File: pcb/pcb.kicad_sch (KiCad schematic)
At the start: 29 parts

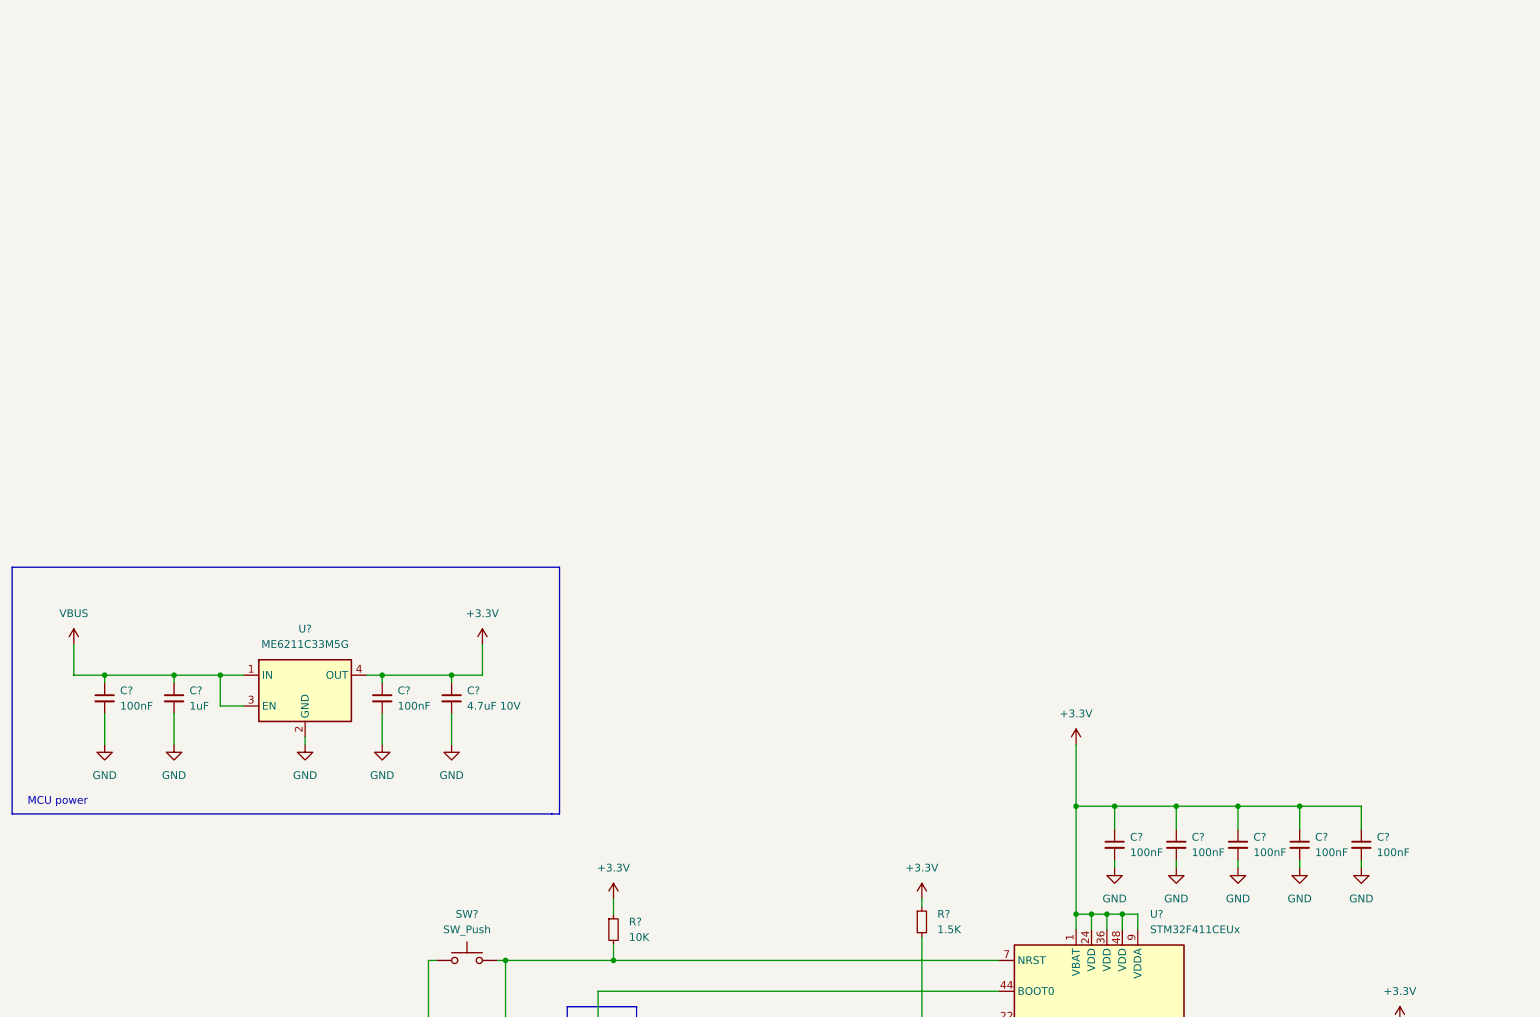
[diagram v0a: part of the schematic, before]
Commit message: add power tree
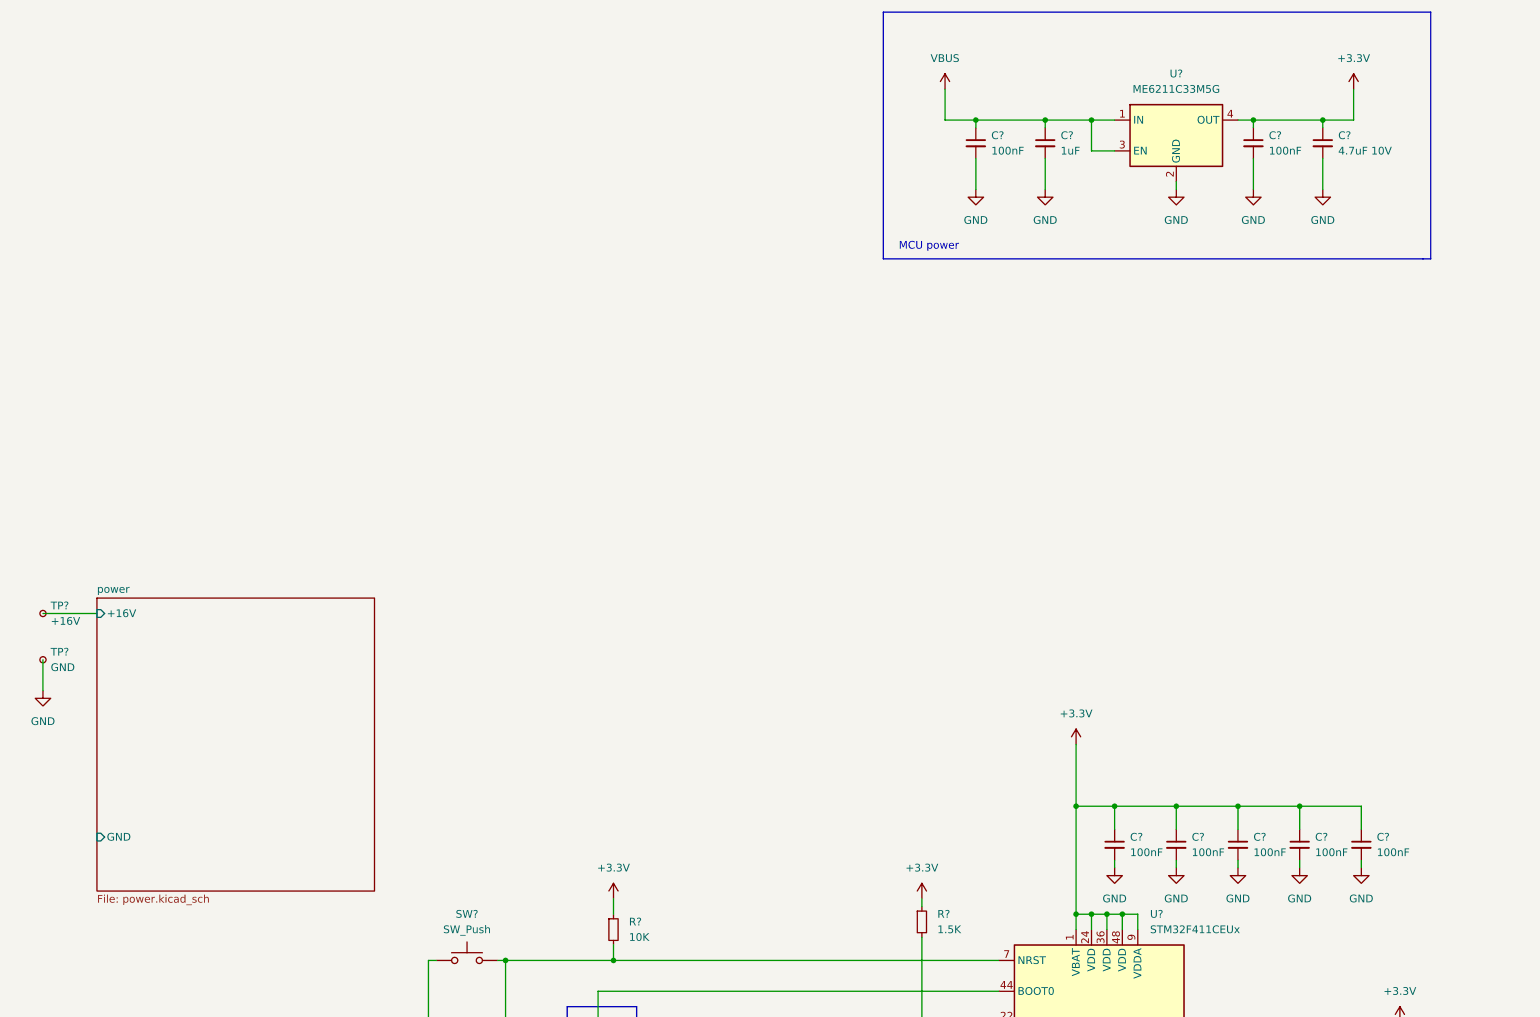
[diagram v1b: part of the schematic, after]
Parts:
- added TP?: GND, symbol Connector:TestPoint_Small
- added TP?: +16V, symbol Connector:TestPoint_Small
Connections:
- net GND: now also TP?.1
- new net power/+16V: TP?.1
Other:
- added sheet power (power.kicad_sch)
- moved on the sheet: C?, U?

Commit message: [temp]
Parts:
- added J? (x2): power amplifier, symbol Connector:Conn_01x03_Female
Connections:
- net GND: now also J?.3 (Pin_3), J?.3 (Pin_3)
- new net power/+15V: J?.1 (Pin_1)
- new net power/+6V: J?.1 (Pin_1)
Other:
- sheet power ports: added +15V, +3.3V, +3.3VA, +6V, -5V; removed none
- company: (none) -> Nanjing wuyou electronic technology company
- title: (none) -> Power
- moved on the sheet: C?, D?, R?, SW?, TP?, U?, Y?

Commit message: [feature] sch finish
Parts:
- removed C?: 4.7uF 10V, symbol Device:C_Small
- removed C?: 1uF, symbol Device:C_Small
- removed C? (x2): 100nF, symbol Device:C_Small
- removed J? (x2): power amplifier, symbol Connector:Conn_01x03_Female
- removed U?: ME6211C33M5G, Package_TO_SOT_SMD:SOT-23-5, symbol Regulator_Linear:ME6211C33M5G
- added C1, C2, C3, C5, C6, C7: 100nF, symbol Device:C_Small
- added J1: attenuator, symbol Connector:Conn_01x10_Female
- added J2: up converter, symbol Connector:Conn_01x07_Female
- added J4: down converter, symbol Connector:Conn_01x02_Female
- added J?: pa power & att, symbol Connector:Conn_01x06_Female
- added Q1, Q2, Q3: FH3415S, symbol Device:Q_PMOS_DGS
- added R15, R16, R17: 10K, symbol Device:R_Small
- added U1, U2, U3: SSP5840ED, Package_SO:SOIC-16W_7.5x10.3mm_P1.27mm, symbol Isolator:ISO7340FC
- U5: renamed from U?; symbol Interface_UART:MAX3491 -> Interface_UART:ADM1491EBR
- gave numbers to parts that had none: 25
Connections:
- net +3.3V: now also C1.1, C2.1, C3.1, U1.1 (VCC1), U2.1 (VCC1), U3.1 (VCC1)
- net GND: now also C1.2, C2.2, C3.2, C5.1, C6.1, C7.1, J2.7 (Pin_7), J4.2 (Pin_2), J?.6 (Pin_6), U1.10 (EN), U1.16 (VCC2), U1.2 (GND1), U1.8 (GND1), U2.10 (EN), U2.16 (VCC2), U2.2 (GND1), U2.8 (GND1), U3.10 (EN), U3.16 (VCC2), U3.2 (GND1), U3.8 (GND1)
- net at U4.10 (PA0): now also Q1.2 (G), R15.2
- net at U4.11 (PA1): now also Q2.2 (G), R16.2
- net at U4.12 (PA2): now also Q3.2 (G), R17.2
- net at U4.13 (PA3): now also J?.2 (Pin_2)
- net at U4.14 (PA4): now also J?.3 (Pin_3)
- net at U4.15 (PA5): now also J?.4 (Pin_4)
- net at U4.16 (PA6): now also J?.5 (Pin_5)
- net PB0: now reaches U4.18 (PB0)
- net PB1: now reaches U4.19 (PB1)
- net PB2: now reaches U4.20 (PB2)
- net PB10: now reaches U4.21 (PB10)
- net PB11: now reaches U4.25 (PB12)
- net PB3: now reaches U4.39 (PB3)
- net PB4: now reaches U4.40 (PB4)
- net PB5: now reaches U4.41 (PB5)
- net PB6: now reaches U4.42 (PB6)
- net PB7: now reaches U4.43 (PB7)
- net PB8: now reaches U4.45 (PB8)
- net PB9: now reaches U4.46 (PB9)
- new net: J1.4 (Pin_4), U1.11 (OUTD)
- new net: J1.3 (Pin_3), U1.12 (OUTC)
- new net: J1.2 (Pin_2), U1.13 (OUTB)
- new net: J1.1 (Pin_1), U1.14 (OUTA)
- new net: J1.10 (Pin_10), U3.13 (OUTB)
- new net: J1.9 (Pin_9), U3.14 (OUTA)
- new net: J4.1 (Pin_1), Q3.1 (D)
- new net: J1.5 (Pin_5), U2.14 (OUTA)
- new net: J1.6 (Pin_6), U2.13 (OUTB)
- new net: J1.7 (Pin_7), U2.12 (OUTC)
- new net: J1.8 (Pin_8), U2.11 (OUTD)
- new net: J2.1 (Pin_1), J2.2 (Pin_2), J2.3 (Pin_3), J2.4 (Pin_4), J2.5 (Pin_5), Q1.1 (D)
- new net: J2.6 (Pin_6), Q2.1 (D)
- new net +15V: J?.1 (Pin_1)
- new net +3.3VA: Q2.3 (S), R16.1
- new net +6V: Q1.3 (S), Q3.3 (S), R15.1, R17.1
- new net -5V: C5.2, C6.2, C7.2, U1.15 (GND2), U1.9 (GND2), U2.15 (GND2), U2.9 (GND2), U3.15 (GND2), U3.9 (GND2)
- new net DIO1: U1.3 (INA)
- new net DIO10: U3.4 (INB)
- new net DIO11: U3.5 (INC)
- new net DIO12: U3.6 (IND)
- new net DIO2: U1.4 (INB)
- new net DIO3: U1.5 (INC)
- new net DIO4: U1.6 (IND)
- new net DIO5: U2.3 (INA)
- new net DIO6: U2.4 (INB)
- new net DIO7: U2.5 (INC)
- new net DIO8: U2.6 (IND)
- new net DIO9: U3.3 (INA)
- no-connect marks 0 -> 13
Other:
- note added: "ATT1"
- note added: "ATT2"
- note added: "PA_SW"
- note added: "SW"
- note removed: "MCU power"
- moved on the sheet: C10, C11, C12, C13, C14, C15, C16, C17, C4, C8, C9, D1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

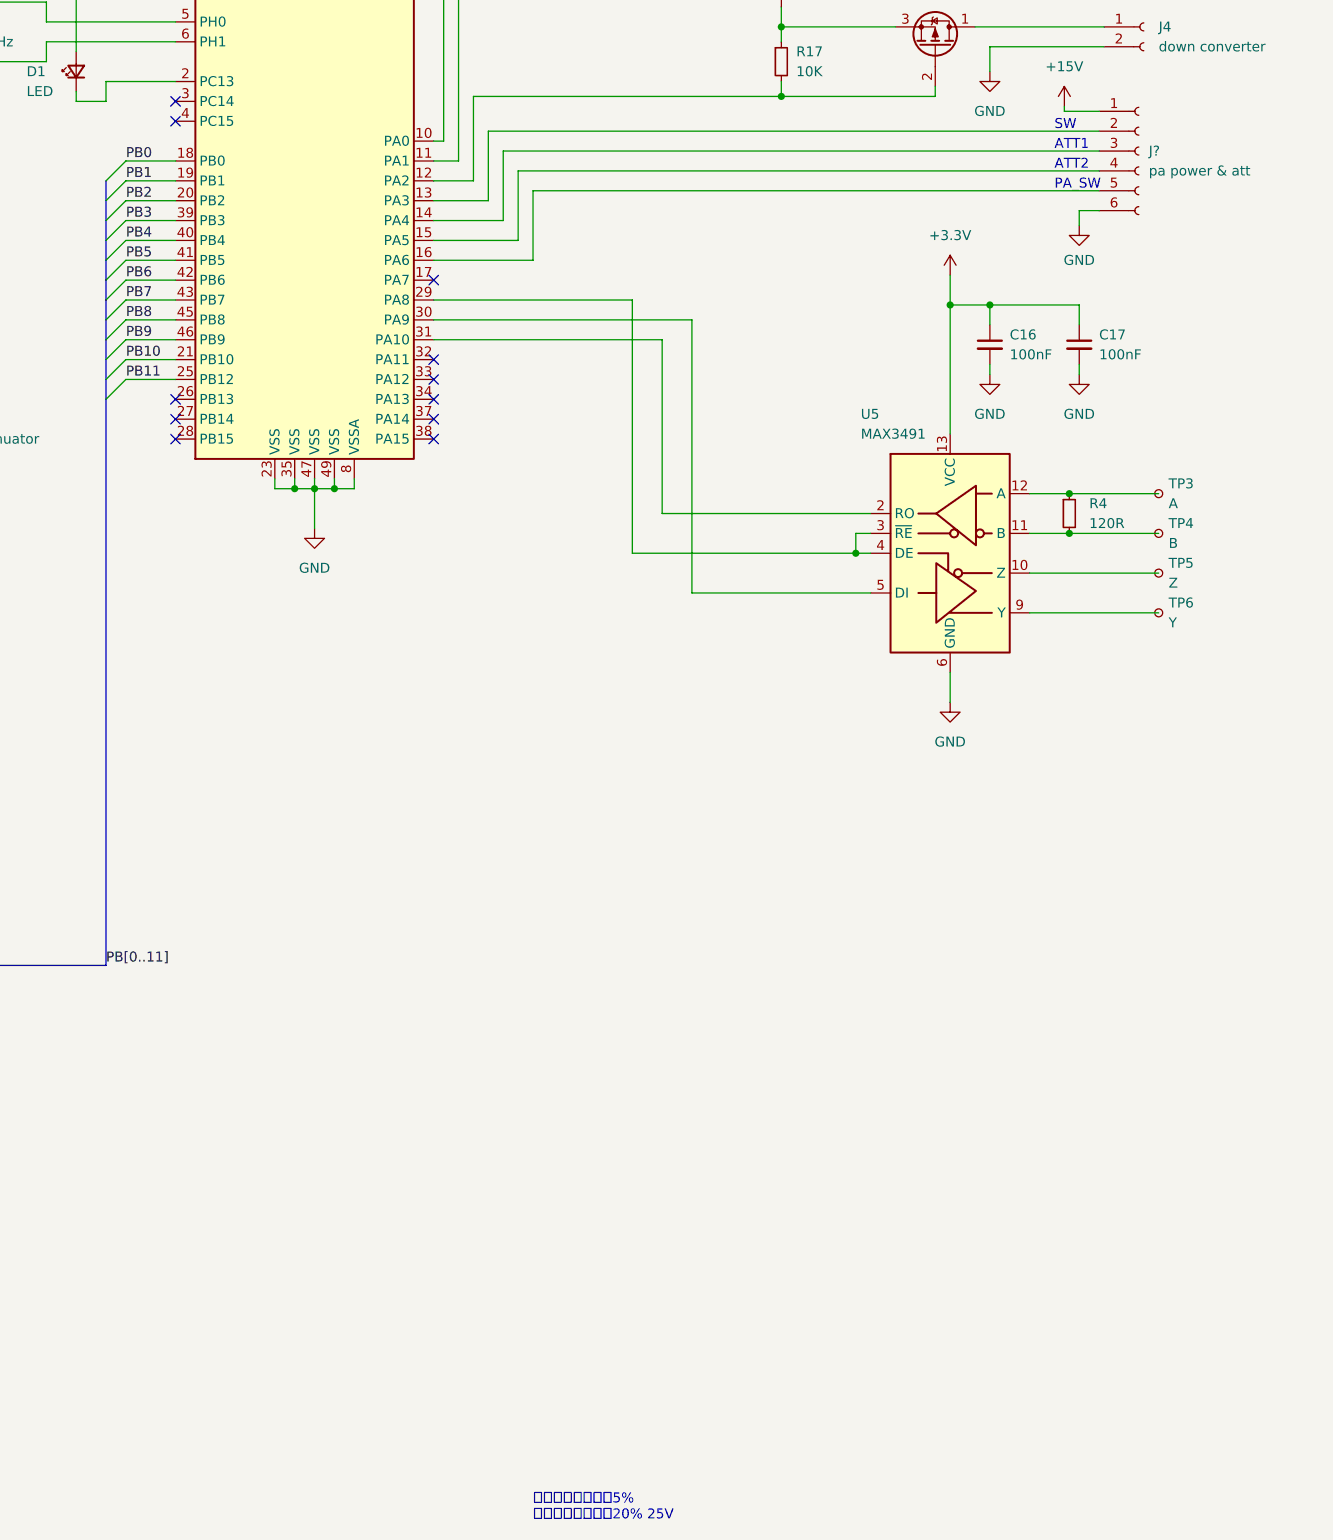
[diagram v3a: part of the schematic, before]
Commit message: [bugfix] fix debug interface and usb
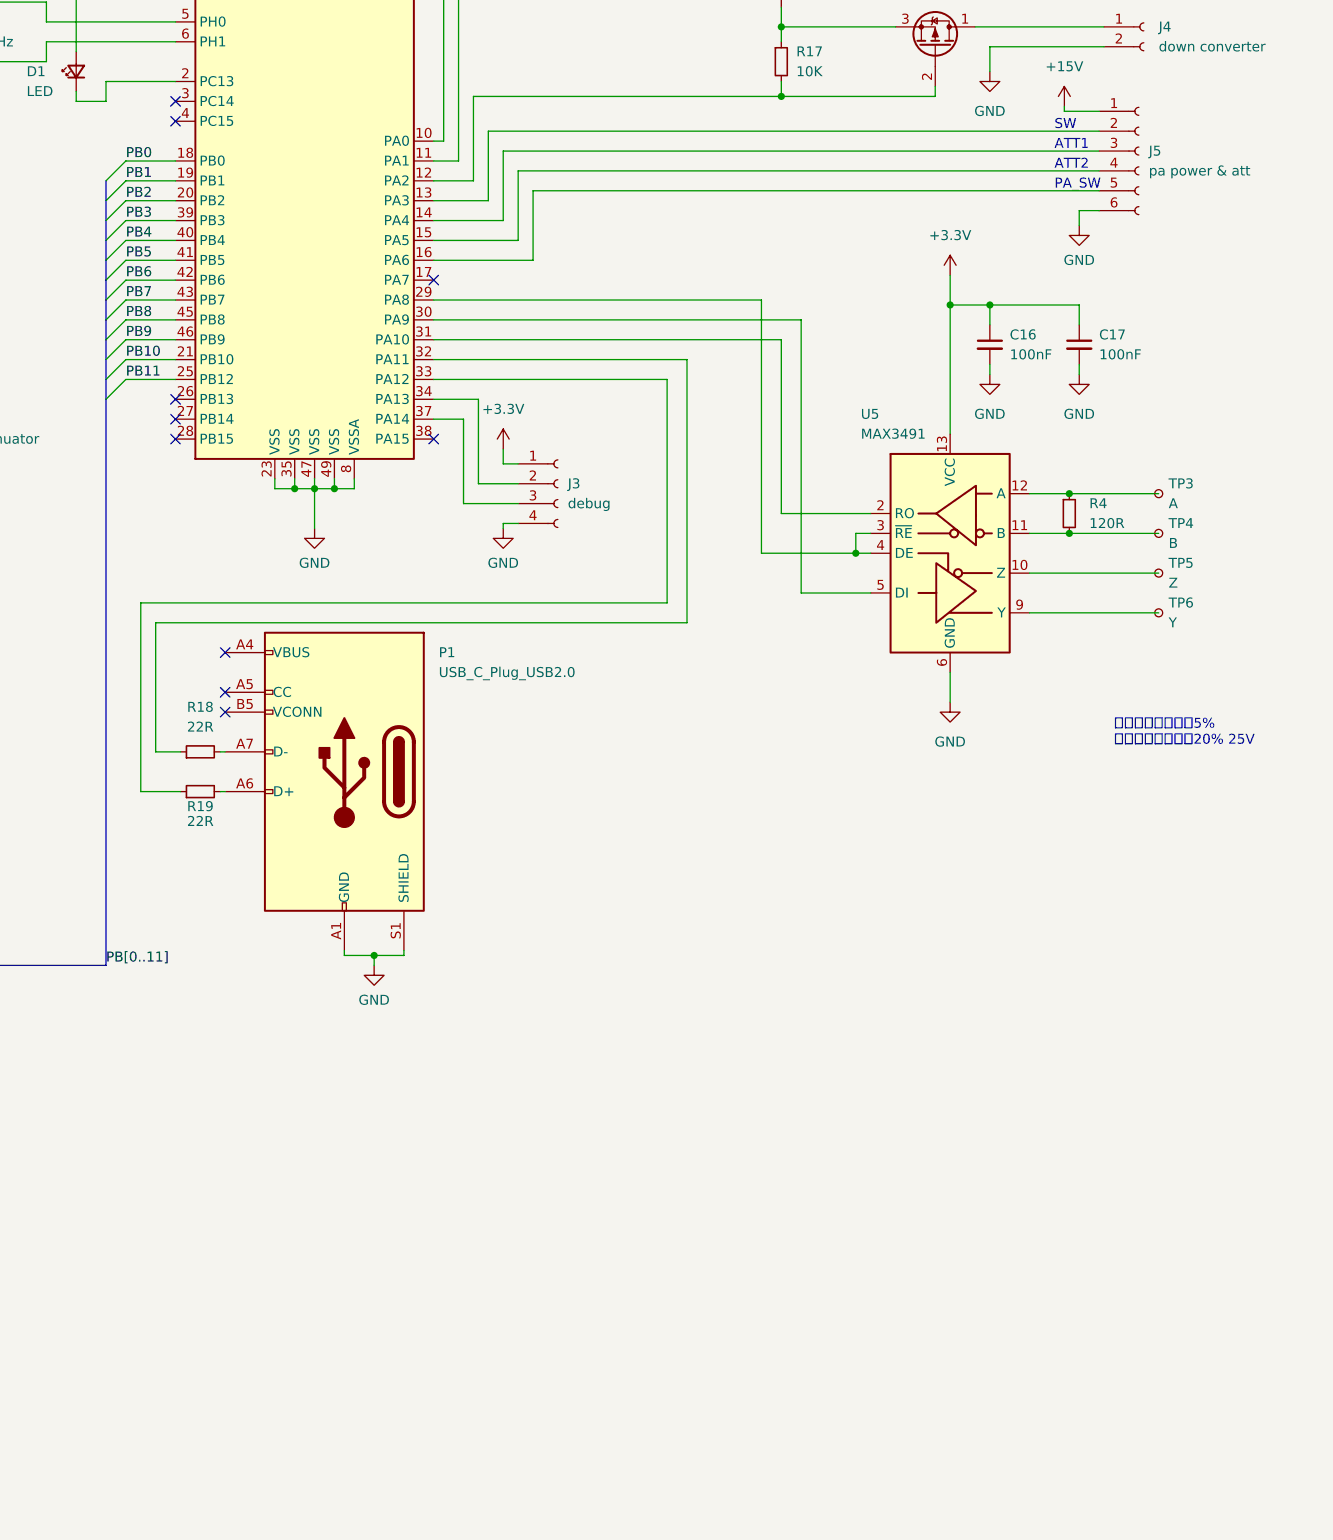
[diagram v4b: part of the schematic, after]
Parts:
- added J3: debug, symbol Connector:Conn_01x04_Female
- added P1: USB_C_Plug_USB2.0, symbol Connector:USB_C_Plug_USB2.0
- added R18, R19: 22R, symbol Device:R_Small
- gave numbers to parts that had none: 1
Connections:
- net +3.3V: now also J3.1 (Pin_1)
- net GND: now also J3.4 (Pin_4), P1.A1 (GND), P1.A12 (GND), P1.B1 (GND), P1.B12 (GND), P1.S1 (SHIELD)
- net at U4.32 (PA11): now also R18.1
- net at U4.33 (PA12): now also R19.1
- net at U4.34 (PA13): now also J3.2 (Pin_2)
- net at U4.37 (PA14): now also J3.3 (Pin_3)
- new net: P1.A4 (VBUS), P1.A9 (VBUS), P1.B4 (VBUS), P1.B9 (VBUS)
- new net: P1.A6 (D+), R19.2
- new net: P1.A7 (D-), R18.2
- no-connect marks 13 -> 12

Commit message: [sch] finish footprint assignment
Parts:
- removed J1: attenuator, symbol Connector:Conn_01x10_Female
- removed J2: up converter, symbol Connector:Conn_01x07_Female
- removed J4: down converter, symbol Connector:Conn_01x02_Female
- removed J5: pa power & att, symbol Connector:Conn_01x06_Female
- added TP10: 4, TestPoint:TestPoint_Pad_2.0x2.0mm, symbol Connector:TestPoint_Small
- added TP11: 5, TestPoint:TestPoint_Pad_2.0x2.0mm, symbol Connector:TestPoint_Small
- added TP12: 6, TestPoint:TestPoint_Pad_2.0x2.0mm, symbol Connector:TestPoint_Small
- added TP13: 7, TestPoint:TestPoint_Pad_2.0x2.0mm, symbol Connector:TestPoint_Small
- added TP14: 8, TestPoint:TestPoint_Pad_2.0x2.0mm, symbol Connector:TestPoint_Small
- added TP15: 9, TestPoint:TestPoint_Pad_2.0x2.0mm, symbol Connector:TestPoint_Small
- added TP16: 10, TestPoint:TestPoint_Pad_2.0x2.0mm, symbol Connector:TestPoint_Small
- added TP17, TP18, TP19, TP20, TP21: 6V, TestPoint:TestPoint_Pad_2.0x2.0mm, symbol Connector:TestPoint_Small
- added TP22: 3.3V, TestPoint:TestPoint_Pad_2.0x2.0mm, symbol Connector:TestPoint_Small
- added TP23, TP29, TP31: GND, TestPoint:TestPoint_Pad_2.0x2.0mm, symbol Connector:TestPoint_Small
- added TP24: +15V, TestPoint:TestPoint_Pad_2.0x2.0mm, symbol Connector:TestPoint_Small
- added TP25: SW, TestPoint:TestPoint_Pad_2.0x2.0mm, symbol Connector:TestPoint_Small
- added TP26: ATT1, TestPoint:TestPoint_Pad_2.0x2.0mm, symbol Connector:TestPoint_Small
- added TP27: ATT2, TestPoint:TestPoint_Pad_2.0x2.0mm, symbol Connector:TestPoint_Small
- added TP28: PA_SW, TestPoint:TestPoint_Pad_2.0x2.0mm, symbol Connector:TestPoint_Small
- added TP30: dc_6v, TestPoint:TestPoint_Pad_2.0x2.0mm, symbol Connector:TestPoint_Small
- added TP7: 1, TestPoint:TestPoint_Pad_2.0x2.0mm, symbol Connector:TestPoint_Small
- added TP8: 2, TestPoint:TestPoint_Pad_2.0x2.0mm, symbol Connector:TestPoint_Small
- added TP9: 3, TestPoint:TestPoint_Pad_2.0x2.0mm, symbol Connector:TestPoint_Small
- C1, C10, C11, C12, C13, C14, C15, C16, C17, C2, C3, C4, C5, C6, C7, C8, C9: footprint (none) -> Capacitor_SMD:C_0603_1608Metric
- D1: footprint (none) -> Diode_SMD:D_0603_1608Metric
- J3: footprint (none) -> Connector_PinHeader_2.54mm:PinHeader_1x04_P2.54mm_Vertical
- P1: footprint (none) -> Connector_USB:USB_C_Receptacle_Amphenol_12401610E4-2A
- Q1, Q2, Q3: footprint (none) -> Package_TO_SOT_SMD:SOT-23
- R1, R15, R16, R17, R18, R19, R2, R3, R4: footprint (none) -> Resistor_SMD:R_0603_1608Metric
- TP1, TP2, TP3, TP4, TP5, TP6: footprint (none) -> TestPoint:TestPoint_Pad_2.0x2.0mm
- Y1: footprint (none) -> Crystal:Crystal_SMD_5032-2Pin_5.0x3.2mm
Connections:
- net +15V: now also TP24.1
- net GND: now also TP23.1, TP29.1, TP31.1
- net at U1.11 (OUTD): now also TP10.1
- net at U1.12 (OUTC): now also TP9.1
- net at U1.13 (OUTB): now also TP8.1
- net at U1.14 (OUTA): now also TP7.1
- net at U4.13 (PA3): now also TP25.1
- net at U4.14 (PA4): now also TP26.1
- net at U4.15 (PA5): now also TP27.1
- net at U4.16 (PA6): now also TP28.1
- net at U3.13 (OUTB): now also TP16.1
- net at U3.14 (OUTA): now also TP15.1
- net at Q3.1 (D): now also TP30.1
- net at U2.14 (OUTA): now also TP11.1
- net at U2.13 (OUTB): now also TP12.1
- net at U2.12 (OUTC): now also TP13.1
- net at U2.11 (OUTD): now also TP14.1
- net at Q1.1 (D): now also TP17.1, TP18.1, TP19.1, TP20.1, TP21.1
- net at Q2.1 (D): now also TP22.1
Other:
- note removed: "ATT1"
- note removed: "ATT2"
- note removed: "PA_SW"
- note removed: "SW"
